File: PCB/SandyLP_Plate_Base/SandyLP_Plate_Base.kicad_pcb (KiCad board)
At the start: 2 copper layers, 275.5 x 80.3 mm, 34 parts

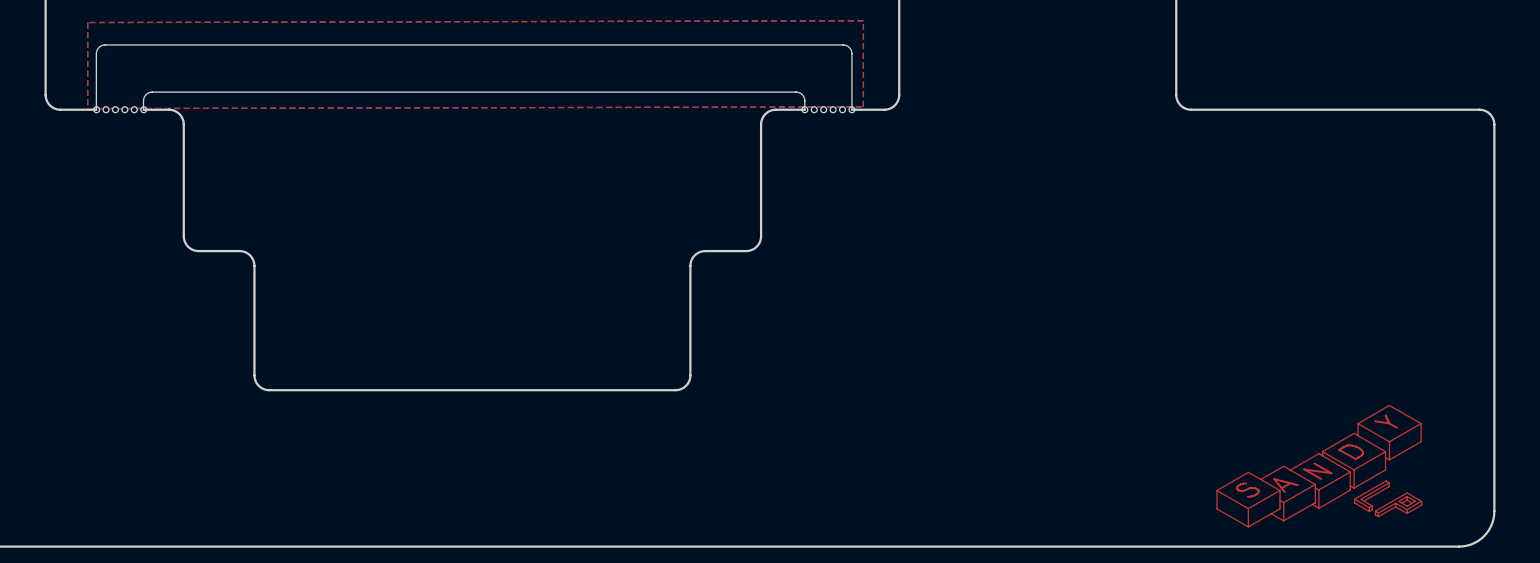
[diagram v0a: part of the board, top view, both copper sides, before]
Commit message: ロータリーエンコーダの穴サイズを縦に拡大
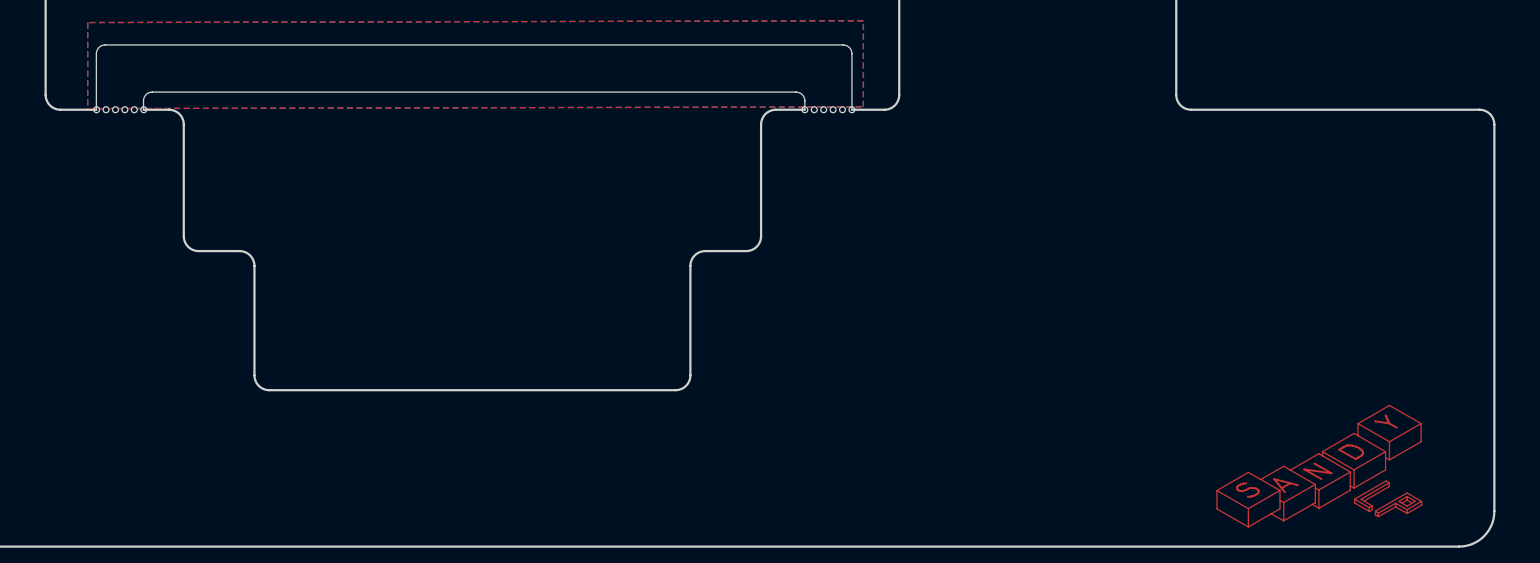
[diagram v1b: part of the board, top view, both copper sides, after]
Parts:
- SW_R5CNT_C1: footprint locallib:MX-Switch-Hole-with-narrow-frame -> locallib:MX-Switch-Hole-for-RE(higher hole)-with-narrow-frame
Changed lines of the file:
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@@
 		(fp_arc
 			(start 88.34 37.54996)
-			(mid 86.925765 36.964177)
+			(mid 86.925801 36.964171)
 			(end 86.34 35.54996)
 			(stroke
@@
 		(fp_arc
 			(start 7.0125 37.785786)
-			(mid 5.598297 37.199991)
+			(mid 5.598293 37.199991)
 			(end 5.0125 35.785786)
 			(stroke
@@
 		(fp_arc
 			(start 88.34 37.54996)
-			(mid 86.925795 36.964148)
+			(mid 86.92583 36.964142)
 			(end 86.34 35.54996)
 			(stroke
@@
 		(fp_arc
 			(start 103.4 37.54996)
-			(mid 104.814192 38.13575)
+			(mid 104.814228 38.135744)
 			(end 105.4 39.54996)
 			(stroke
@@
 		(fp_arc
 			(start 107.4 56.54996)
-			(mid 105.985765 55.964177)
+			(mid 105.985801 55.964171)
 			(end 105.4 54.54996)
 			(stroke
@@
 		(fp_arc
 			(start 112.925 56.54996)
-			(mid 114.339192 57.13575)
+			(mid 114.339228 57.135744)
 			(end 114.925 58.54996)
 			(stroke
@@
 		(fp_arc
 			(start 116.925 75.62496)
-			(mid 115.510765 75.039177)
+			(mid 115.510801 75.039171)
 			(end 114.925 73.62496)
 			(stroke
@@
 		(fp_arc
 			(start 170.85 73.620746)
-			(mid 170.264174 75.034936)
+			(mid 170.264168 75.034901)
 			(end 168.85 75.620746)
 			(stroke
@@
 		(fp_arc
 			(start 180.35 39.471532)
-			(mid 180.935752 38.057304)
+			(mid 180.935746 38.057268)
 			(end 182.35 37.471532)
 			(stroke
@@
 		(fp_arc
 			(start 199.43 35.461532)
-			(mid 198.844179 36.875731)
+			(mid 198.844173 36.875696)
 			(end 197.43 37.461532)
 			(stroke
@@
 		(fp_arc
 			(start 87.325 38.39996)
-			(mid 85.910765 37.814177)
+			(mid 85.910801 37.814171)
 			(end 85.325 36.39996)
 			(stroke
@@
 		(fp_arc
 			(start 92.165554 30.859335)
-			(mid 92.514243 30.017412)
+			(mid 92.514237 30.017377)
 			(end 93.356179 29.66871)
 			(stroke
@@
 		(fp_arc
 			(start 98.515551 37.209335)
-			(mid 98.864241 36.36741)
+			(mid 98.864235 36.367375)
 			(end 99.706179 36.018707)
 			(stroke
@@
 		(fp_arc
 			(start 101.946875 38.39996)
-			(mid 103.361084 38.985741)
+			(mid 103.361119 38.985735)
 			(end 103.946875 40.39996)
 			(stroke
@@
 		(fp_arc
 			(start 105.946875 57.44996)
-			(mid 104.532656 56.864168)
+			(mid 104.532692 56.864162)
 			(end 103.946875 55.44996)
 			(stroke
@@
 		(fp_arc
 			(start 111.471875 57.44996)
-			(mid 112.886084 58.035741)
+			(mid 112.886119 58.035735)
 			(end 113.471875 59.44996)
 			(stroke
@@
 		(fp_arc
 			(start 172.228125 59.44996)
-			(mid 172.813921 58.035746)
+			(mid 172.813927 58.035781)
 			(end 174.228125 57.44996)
 			(stroke
@@
 		(fp_arc
 			(start 181.753125 40.39996)
-			(mid 182.338921 38.985746)
+			(mid 182.338927 38.985781)
 			(end 183.753125 38.39996)
 			(stroke
@@
 		(fp_arc
 			(start 181.753125 55.44996)
-			(mid 181.167348 56.864173)
+			(mid 181.167354 56.864208)
 			(end 179.753125 57.44996)
 			(stroke
@@
 		(fp_arc
 			(start 200.375 36.39996)
-			(mid 199.789222 37.814164)
+			(mid 199.789228 37.814199)
 			(end 198.375 38.39996)
 			(stroke
@@
 		(fp_arc
 			(start 239.7125 38.39996)
-			(mid 238.298301 37.814171)
+			(mid 238.298265 37.814177)
 			(end 237.7125 36.39996)
 			(stroke
@@
 		(fp_arc
 			(start 278.5875 38.39996)
-			(mid 280.001692 38.98575)
+			(mid 280.001728 38.985744)
 			(end 280.5875 40.39996)
 			(stroke
@@
 		)
 	)
-	(footprint "locallib:MX-Switch-Hole-with-narrow-frame"
+	(footprint "locallib:MX-Switch-Hole-for-RE(higher hole)-with-narrow-frame"
 		(layer "F.Cu")
 		(at 159.997345 103.30032)
@@
 			)
 		)
-		(property "Footprint" "locallib:MX-Switch-Hole-with-narrow-frame"
+		(property "Footprint" "locallib:MX-Switch-Hole-for-RE(higher hole)-with-narrow-frame"
 			(at 0 0 0)
 			(unlocked yes)
@@
 		(pad "" np_thru_hole roundrect
 			(at -6.5 0 90)
-			(size 14.8 1.8)
-			(drill oval 14 1)
+			(size 16.3 1.8)
+			(drill oval 15.5 1)
 			(layers "F&B.Cu" "*.Mask")
 			(roundrect_rratio 0.5)
 		)
 		(pad "" np_thru_hole roundrect
-			(at 0 -6.5)
+			(at 0 -7.25)
 			(size 14.8 1.8)
 			(drill oval 14 1)
@@
 		)
 		(pad "" np_thru_hole roundrect
-			(at 0 6.5)
+			(at 0 7.25)
 			(size 14.8 1.8)
 			(drill oval 14 1)
@@
 		(pad "" np_thru_hole roundrect
 			(at 6.5 0 90)
-			(size 14.8 1.8)
-			(drill oval 14 1)
+			(size 16.3 1.8)
+			(drill oval 15.5 1)
 			(layers "F&B.Cu" "*.Mask")
 			(roundrect_rratio 0.5)
 		)
 		(group ""
-			(members "27d7c75c-ec99-44b4-a4ec-6c9e1d3d4548" "9b8504fc-056a-461a-a65d-04eed9f41cc0"
-				"b045c4d9-5c28-46a2-9210-76a3d8228396" "c898f8e2-0f75-47db-817f-daba8611607c"
+			(members "08a45372-0485-461d-82c4-c9a1c2a97a51" "71d46e43-4ee0-4935-912a-5a75b8daf414"
+				"832d28da-42fe-44cf-b743-840b3ae0319a" "c2c33c91-8eb1-4a69-a78f-a1e8d20ee12b"
 			)
 		)

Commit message: ロータリーエンコーダの配置方向を縦から横に変更。
ロータリーエンコーダの端子がプレートに当たるのを回避するようにスイッチプレートの縦を広げると、Base用スイッチプレートの枠が細くなりすぎて強度が足りなくなるため、ロータリーエンコーダの配置方向を変更指定対応した。
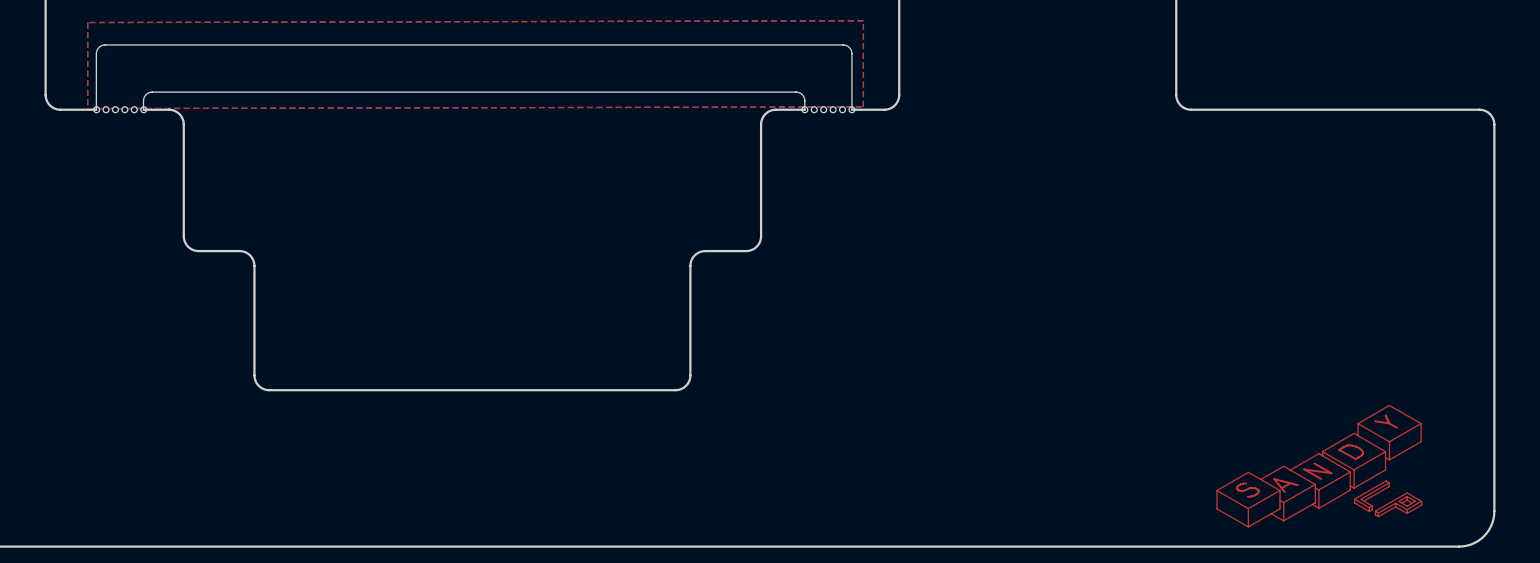
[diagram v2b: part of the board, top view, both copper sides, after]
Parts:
- turned SW_R5CNT_C1 to 90 degrees
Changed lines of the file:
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@@
 		(fp_arc
 			(start 88.34 37.54996)
-			(mid 86.925801 36.964171)
+			(mid 86.925765 36.964177)
 			(end 86.34 35.54996)
 			(stroke
@@
 		(fp_arc
 			(start 7.0125 37.785786)
-			(mid 5.598293 37.199991)
+			(mid 5.598297 37.199991)
 			(end 5.0125 35.785786)
 			(stroke
@@
 		(fp_arc
 			(start 88.34 37.54996)
-			(mid 86.92583 36.964142)
+			(mid 86.925795 36.964148)
 			(end 86.34 35.54996)
 			(stroke
@@
 		(fp_arc
 			(start 103.4 37.54996)
-			(mid 104.814228 38.135744)
+			(mid 104.814192 38.13575)
 			(end 105.4 39.54996)
 			(stroke
@@
 		(fp_arc
 			(start 107.4 56.54996)
-			(mid 105.985801 55.964171)
+			(mid 105.985765 55.964177)
 			(end 105.4 54.54996)
 			(stroke
@@
 		(fp_arc
 			(start 112.925 56.54996)
-			(mid 114.339228 57.135744)
+			(mid 114.339192 57.13575)
 			(end 114.925 58.54996)
 			(stroke
@@
 		(fp_arc
 			(start 116.925 75.62496)
-			(mid 115.510801 75.039171)
+			(mid 115.510765 75.039177)
 			(end 114.925 73.62496)
 			(stroke
@@
 		(fp_arc
 			(start 170.85 73.620746)
-			(mid 170.264168 75.034901)
+			(mid 170.264174 75.034936)
 			(end 168.85 75.620746)
 			(stroke
@@
 		(fp_arc
 			(start 180.35 39.471532)
-			(mid 180.935746 38.057268)
+			(mid 180.935752 38.057304)
 			(end 182.35 37.471532)
 			(stroke
@@
 		(fp_arc
 			(start 199.43 35.461532)
-			(mid 198.844173 36.875696)
+			(mid 198.844179 36.875731)
 			(end 197.43 37.461532)
 			(stroke
@@
 		(fp_arc
 			(start 87.325 38.39996)
-			(mid 85.910801 37.814171)
+			(mid 85.910765 37.814177)
 			(end 85.325 36.39996)
 			(stroke
@@
 		(fp_arc
 			(start 92.165554 30.859335)
-			(mid 92.514237 30.017377)
+			(mid 92.514243 30.017412)
 			(end 93.356179 29.66871)
 			(stroke
@@
 		(fp_arc
 			(start 98.515551 37.209335)
-			(mid 98.864235 36.367375)
+			(mid 98.864241 36.36741)
 			(end 99.706179 36.018707)
 			(stroke
@@
 		(fp_arc
 			(start 101.946875 38.39996)
-			(mid 103.361119 38.985735)
+			(mid 103.361084 38.985741)
 			(end 103.946875 40.39996)
 			(stroke
@@
 		(fp_arc
 			(start 105.946875 57.44996)
-			(mid 104.532692 56.864162)
+			(mid 104.532656 56.864168)
 			(end 103.946875 55.44996)
 			(stroke
@@
 		(fp_arc
 			(start 111.471875 57.44996)
-			(mid 112.886119 58.035735)
+			(mid 112.886084 58.035741)
 			(end 113.471875 59.44996)
 			(stroke
@@
 		(fp_arc
 			(start 172.228125 59.44996)
-			(mid 172.813927 58.035781)
+			(mid 172.813921 58.035746)
 			(end 174.228125 57.44996)
 			(stroke
@@
 		(fp_arc
 			(start 181.753125 40.39996)
-			(mid 182.338927 38.985781)
+			(mid 182.338921 38.985746)
 			(end 183.753125 38.39996)
 			(stroke
@@
 		(fp_arc
 			(start 181.753125 55.44996)
-			(mid 181.167354 56.864208)
+			(mid 181.167348 56.864173)
 			(end 179.753125 57.44996)
 			(stroke
@@
 		(fp_arc
 			(start 200.375 36.39996)
-			(mid 199.789228 37.814199)
+			(mid 199.789222 37.814164)
 			(end 198.375 38.39996)
 			(stroke
@@
 		(fp_arc
 			(start 239.7125 38.39996)
-			(mid 238.298265 37.814177)
+			(mid 238.298301 37.814171)
 			(end 237.7125 36.39996)
 			(stroke
@@
 		(fp_arc
 			(start 278.5875 38.39996)
-			(mid 280.001728 38.985744)
+			(mid 280.001692 38.98575)
 			(end 280.5875 40.39996)
 			(stroke
@@
 	(footprint "locallib:MX-Switch-Hole-for-RE(higher hole)-with-narrow-frame"
 		(layer "F.Cu")
-		(at 159.997345 103.30032)
+		(at 159.997345 103.30032 90)
 		(property "Reference" "SW_R5CNT_C1"
-			(at 0 -0.5 0)
+			(at 0 -0.5 90)
 			(unlocked yes)
 			(layer "F.SilkS")
@@
 		)
 		(property "Value" "RotaryEncoder_Switch"
-			(at 0 1 0)
+			(at 0 1 90)
 			(unlocked yes)
 			(layer "F.Fab")
@@
 		)
 		(property "Footprint" "locallib:MX-Switch-Hole-for-RE(higher hole)-with-narrow-frame"
-			(at 0 0 0)
+			(at 0 0 90)
 			(unlocked yes)
 			(layer "F.Fab")
@@
 		)
 		(property "Datasheet" ""
-			(at 0 0 0)
+			(at 0 0 90)
 			(unlocked yes)
 			(layer "F.Fab")
@@
 		)
 		(property "Description" ""
-			(at 0 0 0)
+			(at 0 0 90)
 			(unlocked yes)
 			(layer "F.Fab")
@@
 		(attr through_hole)
 		(fp_line
-			(start -9.525 -9.525)
-			(end 9.525 -9.525)
+			(start 9.525 -9.525)
+			(end 9.525 9.525)
 			(stroke
 				(width 0.15)
@@
 		)
 		(fp_line
-			(start -9.525 9.525)
-			(end -9.525 -9.525)
+			(start -9.525 -9.525)
+			(end 9.525 -9.525)
 			(stroke
 				(width 0.15)
@@
 		)
 		(fp_line
-			(start 9.525 -9.525)
-			(end 9.525 9.525)
+			(start 9.525 9.525)
+			(end -9.525 9.525)
 			(stroke
 				(width 0.15)
@@
 		)
 		(fp_line
-			(start 9.525 9.525)
-			(end -9.525 9.525)
+			(start -9.525 9.525)
+			(end -9.525 -9.525)
 			(stroke
 				(width 0.15)
@@
 		)
 		(pad "" np_thru_hole roundrect
-			(at -6.5 0 90)
-			(size 16.3 1.8)
-			(drill oval 15.5 1)
+			(at -6.5 0 180)
+			(size 17.3 1.8)
+			(drill oval 16.5 1)
 			(layers "F&B.Cu" "*.Mask")
 			(roundrect_rratio 0.5)
 		)
 		(pad "" np_thru_hole roundrect
-			(at 0 -7.25)
+			(at 0 -7.75 90)
 			(size 14.8 1.8)
 			(drill oval 14 1)
@@
 		)
 		(pad "" np_thru_hole roundrect
-			(at 0 7.25)
+			(at 0 7.75 90)
 			(size 14.8 1.8)
 			(drill oval 14 1)
@@
 		)
 		(pad "" np_thru_hole roundrect
-			(at 6.5 0 90)
-			(size 16.3 1.8)
-			(drill oval 15.5 1)
+			(at 6.5 0 180)
+			(size 17.3 1.8)
+			(drill oval 16.5 1)
 			(layers "F&B.Cu" "*.Mask")
 			(roundrect_rratio 0.5)
 		)
 		(group ""
-			(members "08a45372-0485-461d-82c4-c9a1c2a97a51" "71d46e43-4ee0-4935-912a-5a75b8daf414"
-				"832d28da-42fe-44cf-b743-840b3ae0319a" "c2c33c91-8eb1-4a69-a78f-a1e8d20ee12b"
+			(members "641adc22-7fa4-4661-8873-885efd523a83" "6d632c8f-16e5-4c18-b5d8-e7508ea235f8"
+				"984dea1b-ef48-4e65-a9f7-a294cb1bbbcf" "ca803163-850b-4281-9881-352256a17066"
 			)
 		)

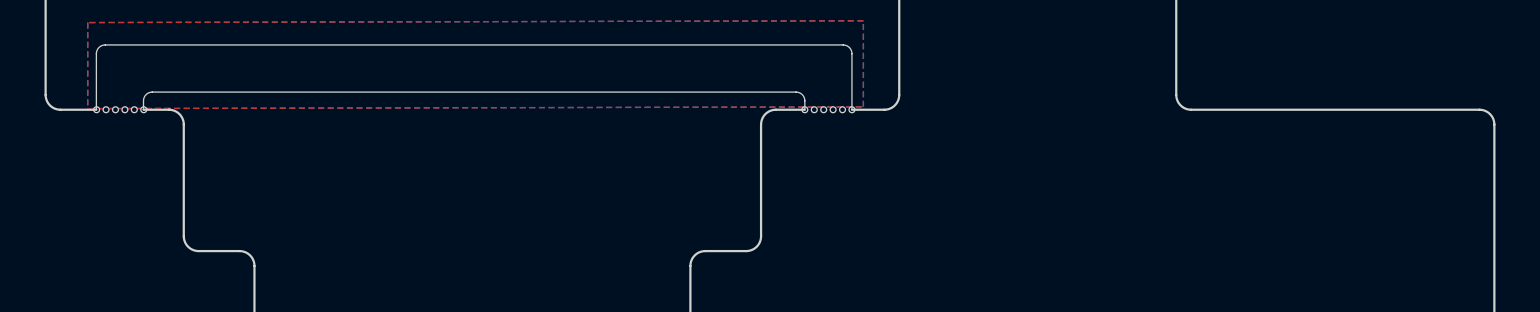
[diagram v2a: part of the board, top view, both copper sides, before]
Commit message: オプションが無料になったのでJLCのマーキングを削除。その他シルク位置調整。
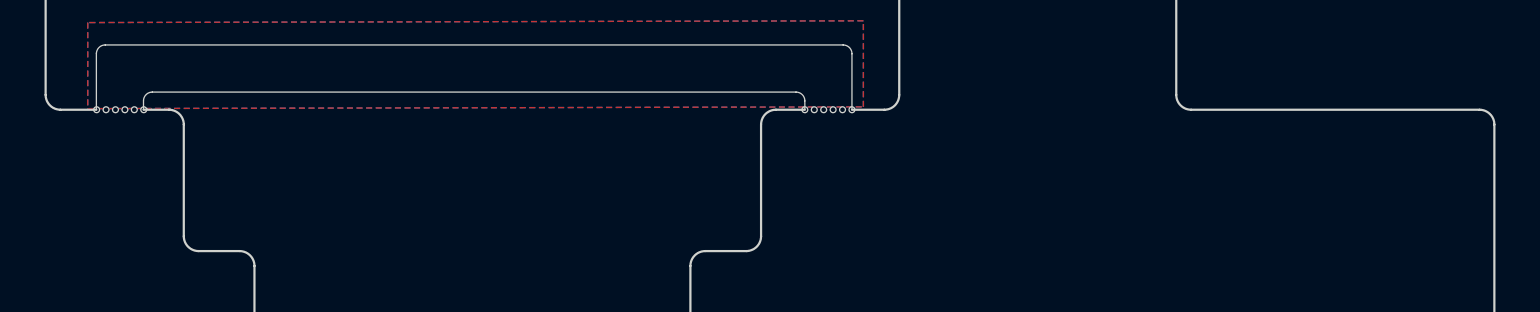
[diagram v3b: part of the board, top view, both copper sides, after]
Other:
- board text added: "#SandyLP_kbd"
- board text added: "DN0010"
- board text added: "Plate for Base"
- board text added: "by @jpskenn"
- board text removed: "#SandyLP_kbd DN0010, Plate for Base by @jpskenn"
- board text removed: "JLCJLCJLCJLC"
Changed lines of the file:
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@@
 		(fp_arc
 			(start 88.34 37.54996)
-			(mid 86.925765 36.964177)
+			(mid 86.925801 36.964171)
 			(end 86.34 35.54996)
 			(stroke
@@
 		(fp_arc
 			(start 7.0125 37.785786)
-			(mid 5.598297 37.199991)
+			(mid 5.598293 37.199991)
 			(end 5.0125 35.785786)
 			(stroke
@@
 		(fp_arc
 			(start 88.34 37.54996)
-			(mid 86.925795 36.964148)
+			(mid 86.92583 36.964142)
 			(end 86.34 35.54996)
 			(stroke
@@
 		(fp_arc
 			(start 103.4 37.54996)
-			(mid 104.814192 38.13575)
+			(mid 104.814228 38.135744)
 			(end 105.4 39.54996)
 			(stroke
@@
 		(fp_arc
 			(start 107.4 56.54996)
-			(mid 105.985765 55.964177)
+			(mid 105.985801 55.964171)
 			(end 105.4 54.54996)
 			(stroke
@@
 		(fp_arc
 			(start 112.925 56.54996)
-			(mid 114.339192 57.13575)
+			(mid 114.339228 57.135744)
 			(end 114.925 58.54996)
 			(stroke
@@
 		(fp_arc
 			(start 116.925 75.62496)
-			(mid 115.510765 75.039177)
+			(mid 115.510801 75.039171)
 			(end 114.925 73.62496)
 			(stroke
@@
 		(fp_arc
 			(start 170.85 73.620746)
-			(mid 170.264174 75.034936)
+			(mid 170.264168 75.034901)
 			(end 168.85 75.620746)
 			(stroke
@@
 		(fp_arc
 			(start 180.35 39.471532)
-			(mid 180.935752 38.057304)
+			(mid 180.935746 38.057268)
 			(end 182.35 37.471532)
 			(stroke
@@
 		(fp_arc
 			(start 199.43 35.461532)
-			(mid 198.844179 36.875731)
+			(mid 198.844173 36.875696)
 			(end 197.43 37.461532)
 			(stroke
@@
 		(fp_arc
 			(start 87.325 38.39996)
-			(mid 85.910765 37.814177)
+			(mid 85.910801 37.814171)
 			(end 85.325 36.39996)
 			(stroke
@@
 		(fp_arc
 			(start 92.165554 30.859335)
-			(mid 92.514243 30.017412)
+			(mid 92.514237 30.017377)
 			(end 93.356179 29.66871)
 			(stroke
@@
 		(fp_arc
 			(start 98.515551 37.209335)
-			(mid 98.864241 36.36741)
+			(mid 98.864235 36.367375)
 			(end 99.706179 36.018707)
 			(stroke
@@
 		(fp_arc
 			(start 101.946875 38.39996)
-			(mid 103.361084 38.985741)
+			(mid 103.361119 38.985735)
 			(end 103.946875 40.39996)
 			(stroke
@@
 		(fp_arc
 			(start 105.946875 57.44996)
-			(mid 104.532656 56.864168)
+			(mid 104.532692 56.864162)
 			(end 103.946875 55.44996)
 			(stroke
@@
 		(fp_arc
 			(start 111.471875 57.44996)
-			(mid 112.886084 58.035741)
+			(mid 112.886119 58.035735)
 			(end 113.471875 59.44996)
 			(stroke
@@
 		(fp_arc
 			(start 172.228125 59.44996)
-			(mid 172.813921 58.035746)
+			(mid 172.813927 58.035781)
 			(end 174.228125 57.44996)
 			(stroke
@@
 		(fp_arc
 			(start 181.753125 40.39996)
-			(mid 182.338921 38.985746)
+			(mid 182.338927 38.985781)
 			(end 183.753125 38.39996)
 			(stroke
@@
 		(fp_arc
 			(start 181.753125 55.44996)
-			(mid 181.167348 56.864173)
+			(mid 181.167354 56.864208)
 			(end 179.753125 57.44996)
 			(stroke
@@
 		(fp_arc
 			(start 200.375 36.39996)
-			(mid 199.789222 37.814164)
+			(mid 199.789228 37.814199)
 			(end 198.375 38.39996)
 			(stroke
@@
 		(fp_arc
 			(start 239.7125 38.39996)
-			(mid 238.298301 37.814171)
+			(mid 238.298265 37.814177)
 			(end 237.7125 36.39996)
 			(stroke
@@
 		(fp_arc
 			(start 278.5875 38.39996)
-			(mid 280.001692 38.98575)
+			(mid 280.001728 38.985744)
 			(end 280.5875 40.39996)
 			(stroke
@@
 		)
 	)
-	(gr_text "#SandyLP_kbd DN0010, Plate for Base by @jpskenn"
-		(at 120.70672 58.05657 0)
+	(gr_text "DN0010"
+		(at 83.797345 76.24407 0)
 		(layer "B.SilkS")
 		(effects
@@
 				(thickness 0.15)
 			)
-			(justify left bottom mirror)
+			(justify bottom mirror)
 		)
 	)
-	(gr_text "JLCJLCJLCJLC"
-		(at 212.384845 58.05657 0)
+	(gr_text "Plate for Base"
+		(at 64.747345 76.24407 0)
 		(layer "B.SilkS")
 		(effects
@@
 				(thickness 0.15)
 			)
-			(justify left bottom mirror)
+			(justify bottom mirror)
+		)
+	)
+	(gr_text "#SandyLP_kbd"
+		(at 102.847345 76.24407 0)
+		(layer "B.SilkS")
+		(effects
+			(font
+				(size 1 1)
+				(thickness 0.15)
+			)
+			(justify bottom mirror)
+		)
+	)
+	(gr_text "by @jpskenn"
+		(at 45.697345 76.24407 0)
+		(layer "B.SilkS")
+		(effects
+			(font
+				(size 1 1)
+				(thickness 0.15)
+			)
+			(justify bottom mirror)
 		)
 	)

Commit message: ロゴ更新
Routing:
- net (no net): track 237.9 -> 236.8 mm
